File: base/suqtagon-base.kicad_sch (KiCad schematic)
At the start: 24 parts, among them J1 USB_C_Receptacle_USB2.0, J2 Conn_01x02_Male, J3 Conn_01x02_Male, J4 Conn_01x02_Male, J5 Conn_01x02_Male, J6 Conn_01x02_Male, SW1 SW_Push, SW2 SW_Push, U1 AMS1117-3.3

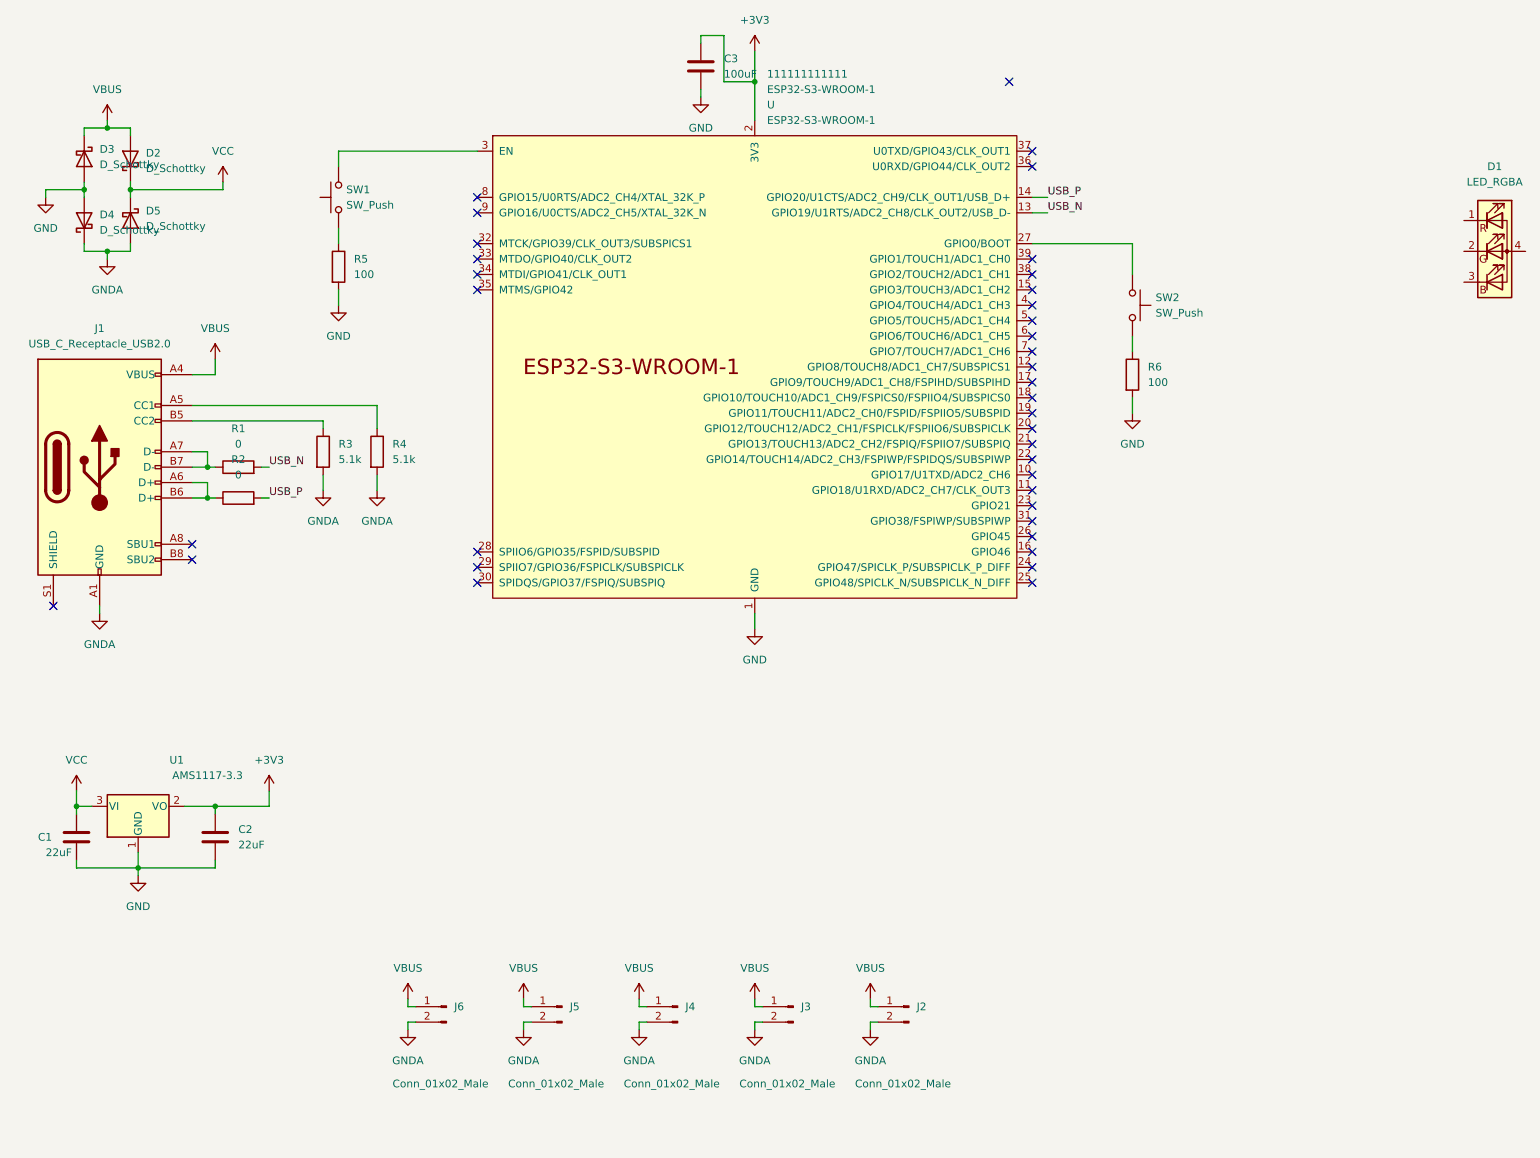
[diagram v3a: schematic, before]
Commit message: started adding hand solder footprints
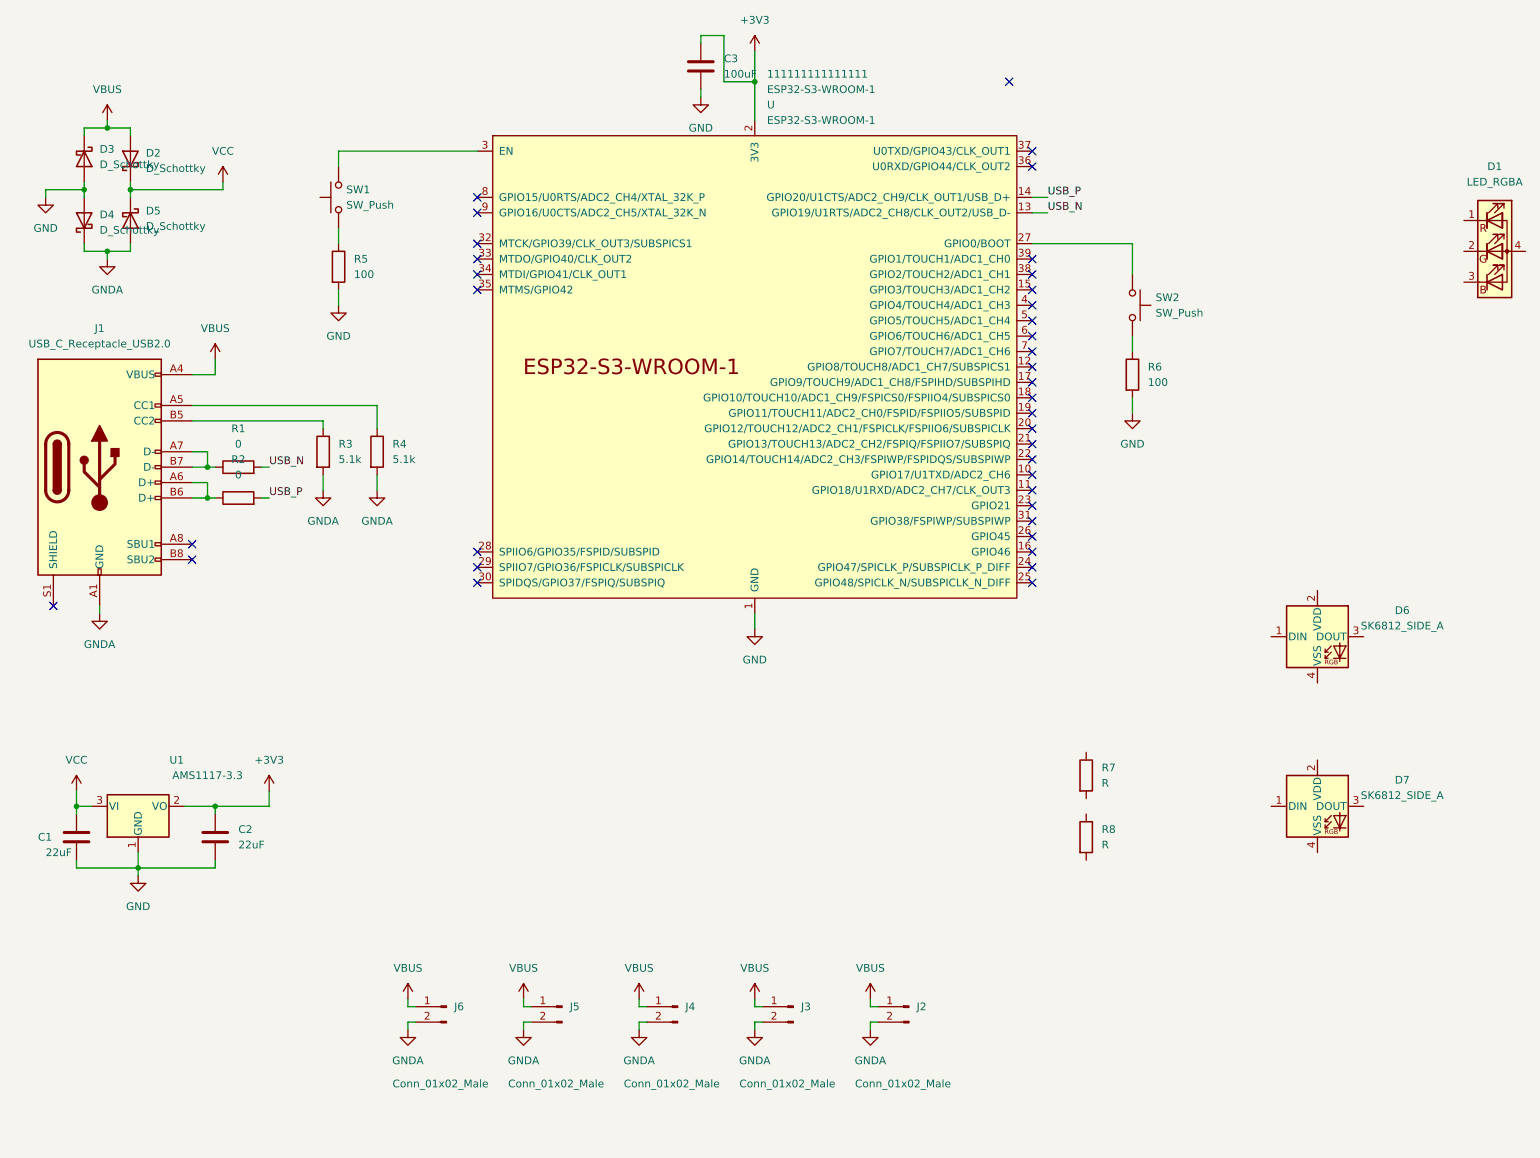
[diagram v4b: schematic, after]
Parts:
- added D6, D7: SK6812_SIDE_A, LED_SMD_SIDE:LED_SMD_SK6812_SIDE_A_4020, symbol LED_Side:SK6812_SIDE_A
- added R7: R, Resistor_SMD:R_0805_2012Metric, symbol Device:R
- added R8: R, Resistor_SMD:R_0805_2012Metric_Pad1.20x1.40mm_HandSolder, symbol Device:R
- renumbered 111111111111 to 111111111111111
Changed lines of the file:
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@@
     (effects (font (size 1.27 1.27)) (justify left bottom))
+  )
+  (symbol (lib_id "LED_Side:SK6812_SIDE_A") (at 232.41 114.3 0) (unit 1)
+    (in_bom yes) (on_board yes) (fields_autoplaced)
+    (property "Reference" "D6" (id 0) (at 246.38 109.9693 0))
+    (property "Value" "SK6812_SIDE_A" (id 1) (at 246.38 112.5093 0))
+    (property "Footprint" "LED_SMD_SIDE:LED_SMD_SK6812_SIDE_A_4020" (id 2) (at 233.68 121.92 0)
+      (effects (font (size 1.27 1.27)) (justify left top) hide)
+    )
+    (property "Datasheet" "http://www.normandled.com/upload/201810/SK6812%20SIDE-A%20LED%20Datasheet.pdf" (id 3) (at 234.95 123.825 0)
+      (effects (font (size 1.27 1.27)) (justify left top) hide)
+    )
+    (pin "1")
+    (pin "2")
+    (pin "3")
+    (pin "4")
   )
   (symbol (lib_id "power:GNDA") (at 68.58 90.17 0) (unit 1)
@@
     (pin "2")
   )
+  (symbol (lib_id "Device:R") (at 194.31 137.16 0) (unit 1)
+    (in_bom yes) (on_board yes) (fields_autoplaced)
+    (property "Reference" "R7" (id 0) (at 196.85 135.8899 0)
+      (effects (font (size 1.27 1.27)) (justify left))
+    )
+    (property "Value" "R" (id 1) (at 196.85 138.4299 0)
+      (effects (font (size 1.27 1.27)) (justify left))
+    )
+    (property "Footprint" "Resistor_SMD:R_0805_2012Metric" (id 2) (at 192.532 137.16 90)
+      (effects (font (size 1.27 1.27)) hide)
+    )
+    (property "Datasheet" "~" (id 3) (at 194.31 137.16 0)
+      (effects (font (size 1.27 1.27)) hide)
+    )
+    (pin "1")
+    (pin "2")
+  )
   (symbol (lib_id "power:VCC") (at 52.07 39.37 0) (unit 1)
     (in_bom yes) (on_board yes) (fields_autoplaced)
@@
     (pin "2")
   )
+  (symbol (lib_id "Device:R") (at 194.31 147.32 0) (unit 1)
+    (in_bom yes) (on_board yes) (fields_autoplaced)
+    (property "Reference" "R8" (id 0) (at 196.85 146.0499 0)
+      (effects (font (size 1.27 1.27)) (justify left))
+    )
+    (property "Value" "R" (id 1) (at 196.85 148.5899 0)
+      (effects (font (size 1.27 1.27)) (justify left))
+    )
+    (property "Footprint" "Resistor_SMD:R_0805_2012Metric_Pad1.20x1.40mm_HandSolder" (id 2) (at 192.532 147.32 90)
+      (effects (font (size 1.27 1.27)) hide)
+    )
+    (property "Datasheet" "~" (id 3) (at 194.31 147.32 0)
+      (effects (font (size 1.27 1.27)) hide)
+    )
+    (pin "1")
+    (pin "2")
+  )
   (symbol (lib_id "power:VBUS") (at 101.6 173.99 0) (unit 1)
     (in_bom yes) (on_board yes) (fields_autoplaced)
@@
   (symbol (lib_id "Espressif:ESP32-S3-WROOM-1") (at 139.7 69.85 0) (unit 1)
     (in_bom yes) (on_board yes) (fields_autoplaced)
-    (property "Reference" "111111111111" (id 0) (at 141.7194 21.59 0)
+    (property "Reference" "111111111111111" (id 0) (at 141.7194 21.59 0)
       (effects (font (size 1.27 1.27)) (justify left))
     )
@@
     (pin "2")
   )
+  (symbol (lib_id "LED_Side:SK6812_SIDE_A") (at 232.41 142.24 0) (unit 1)
+    (in_bom yes) (on_board yes) (fields_autoplaced)
+    (property "Reference" "D7" (id 0) (at 246.38 137.9093 0))
+    (property "Value" "SK6812_SIDE_A" (id 1) (at 246.38 140.4493 0))
+    (property "Footprint" "LED_SMD_SIDE:LED_SMD_SK6812_SIDE_A_4020" (id 2) (at 233.68 149.86 0)
+      (effects (font (size 1.27 1.27)) (justify left top) hide)
+    )
+    (property "Datasheet" "http://www.normandled.com/upload/201810/SK6812%20SIDE-A%20LED%20Datasheet.pdf" (id 3) (at 234.95 151.765 0)
+      (effects (font (size 1.27 1.27)) (justify left top) hide)
+    )
+    (pin "1")
+    (pin "2")
+    (pin "3")
+    (pin "4")
+  )
   (symbol (lib_id "Connector:Conn_01x02_Male") (at 127 175.26 0) (mirror y) (unit 1)
     (in_bom yes) (on_board yes)
@@
     )
     (path "/761644a8-58a9-4bb2-8003-7f19d43a1827"
-      (reference "111111111111") (unit 1) (value "ESP32-S3-WROOM-1") (footprint "Espressif:ESP32-S3-WROOM-1U")
+      (reference "111111111111111") (unit 1) (value "ESP32-S3-WROOM-1") (footprint "Espressif:ESP32-S3-WROOM-1U")
     )
     (path "/1062990a-607a-4b52-b57c-c444e6f10a17"
@@
       (reference "D5") (unit 1) (value "D_Schottky") (footprint "Diode_SMD:D_SMB")
     )
+    (path "/05584861-80b0-4823-89c5-d677033aeb10"
+      (reference "D6") (unit 1) (value "SK6812_SIDE_A") (footprint "LED_SMD_SIDE:LED_SMD_SK6812_SIDE_A_4020")
+    )
+    (path "/dac5b6f8-e0f5-4896-bd9d-ba13c95e5a2b"
+      (reference "D7") (unit 1) (value "SK6812_SIDE_A") (footprint "LED_SMD_SIDE:LED_SMD_SK6812_SIDE_A_4020")
+    )
     (path "/d1f6cfad-2a05-4c1b-99fc-73c0e2e6741a"
       (reference "J1") (unit 1) (value "USB_C_Receptacle_USB2.0") (footprint "Connector_USB:USB_C_Receptacle_HRO_TYPE-C-31-M-12")
@@
       (reference "R6") (unit 1) (value "100") (footprint "Resistor_SMD:R_0805_2012Metric_Pad1.20x1.40mm_HandSolder")
     )
+    (path "/09669309-32ea-4a5f-92b3-fed51f6e2892"
+      (reference "R7") (unit 1) (value "R") (footprint "Resistor_SMD:R_0805_2012Metric")
+    )
+    (path "/598a8726-a9f0-4383-83de-07a648077382"
+      (reference "R8") (unit 1) (value "R") (footprint "Resistor_SMD:R_0805_2012Metric_Pad1.20x1.40mm_HandSolder")
+    )
     (path "/b1083b2b-afcd-4f5b-a5a9-2da0cdfd2a2f"

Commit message: test background eb
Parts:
- removed R7: R, Resistor_SMD:R_0805_2012Metric, symbol Device:R
- removed R8: R, Resistor_SMD:R_0805_2012Metric_Pad1.20x1.40mm_HandSolder, symbol Device:R
- D6, D7: footprint LED_SMD_SIDE:LED_SMD_SK6812_SIDE_A_4020 -> LED_SMD_SIDE:LED_SMD_SK6812_SIDE_A_4020_HandSolder
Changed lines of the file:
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@@
     (property "Reference" "D6" (id 0) (at 246.38 109.9693 0))
     (property "Value" "SK6812_SIDE_A" (id 1) (at 246.38 112.5093 0))
-    (property "Footprint" "LED_SMD_SIDE:LED_SMD_SK6812_SIDE_A_4020" (id 2) (at 233.68 121.92 0)
+    (property "Footprint" "LED_SMD_SIDE:LED_SMD_SK6812_SIDE_A_4020_HandSolder" (id 2) (at 233.68 121.92 0)
       (effects (font (size 1.27 1.27)) (justify left top) hide)
     )
@@
     (pin "2")
   )
-  (symbol (lib_id "Device:R") (at 194.31 137.16 0) (unit 1)
-    (in_bom yes) (on_board yes) (fields_autoplaced)
-    (property "Reference" "R7" (id 0) (at 196.85 135.8899 0)
-      (effects (font (size 1.27 1.27)) (justify left))
-    )
-    (property "Value" "R" (id 1) (at 196.85 138.4299 0)
-      (effects (font (size 1.27 1.27)) (justify left))
-    )
-    (property "Footprint" "Resistor_SMD:R_0805_2012Metric" (id 2) (at 192.532 137.16 90)
-      (effects (font (size 1.27 1.27)) hide)
-    )
-    (property "Datasheet" "~" (id 3) (at 194.31 137.16 0)
-      (effects (font (size 1.27 1.27)) hide)
-    )
-    (pin "1")
-    (pin "2")
-  )
   (symbol (lib_id "power:VCC") (at 52.07 39.37 0) (unit 1)
     (in_bom yes) (on_board yes) (fields_autoplaced)
@@
     )
     (property "Datasheet" "~" (id 3) (at 77.47 83.82 0)
-      (effects (font (size 1.27 1.27)) hide)
-    )
-    (pin "1")
-    (pin "2")
-  )
-  (symbol (lib_id "Device:R") (at 194.31 147.32 0) (unit 1)
-    (in_bom yes) (on_board yes) (fields_autoplaced)
-    (property "Reference" "R8" (id 0) (at 196.85 146.0499 0)
-      (effects (font (size 1.27 1.27)) (justify left))
-    )
-    (property "Value" "R" (id 1) (at 196.85 148.5899 0)
-      (effects (font (size 1.27 1.27)) (justify left))
-    )
-    (property "Footprint" "Resistor_SMD:R_0805_2012Metric_Pad1.20x1.40mm_HandSolder" (id 2) (at 192.532 147.32 90)
-      (effects (font (size 1.27 1.27)) hide)
-    )
-    (property "Datasheet" "~" (id 3) (at 194.31 147.32 0)
       (effects (font (size 1.27 1.27)) hide)
     )
@@
     (property "Reference" "D7" (id 0) (at 246.38 137.9093 0))
     (property "Value" "SK6812_SIDE_A" (id 1) (at 246.38 140.4493 0))
-    (property "Footprint" "LED_SMD_SIDE:LED_SMD_SK6812_SIDE_A_4020" (id 2) (at 233.68 149.86 0)
+    (property "Footprint" "LED_SMD_SIDE:LED_SMD_SK6812_SIDE_A_4020_HandSolder" (id 2) (at 233.68 149.86 0)
       (effects (font (size 1.27 1.27)) (justify left top) hide)
     )
@@
     )
     (path "/05584861-80b0-4823-89c5-d677033aeb10"
-      (reference "D6") (unit 1) (value "SK6812_SIDE_A") (footprint "LED_SMD_SIDE:LED_SMD_SK6812_SIDE_A_4020")
+      (reference "D6") (unit 1) (value "SK6812_SIDE_A") (footprint "LED_SMD_SIDE:LED_SMD_SK6812_SIDE_A_4020_HandSolder")
     )
     (path "/dac5b6f8-e0f5-4896-bd9d-ba13c95e5a2b"
-      (reference "D7") (unit 1) (value "SK6812_SIDE_A") (footprint "LED_SMD_SIDE:LED_SMD_SK6812_SIDE_A_4020")
+      (reference "D7") (unit 1) (value "SK6812_SIDE_A") (footprint "LED_SMD_SIDE:LED_SMD_SK6812_SIDE_A_4020_HandSolder")
     )
     (path "/d1f6cfad-2a05-4c1b-99fc-73c0e2e6741a"
@@
       (reference "R6") (unit 1) (value "100") (footprint "Resistor_SMD:R_0805_2012Metric_Pad1.20x1.40mm_HandSolder")
     )
-    (path "/09669309-32ea-4a5f-92b3-fed51f6e2892"
-      (reference "R7") (unit 1) (value "R") (footprint "Resistor_SMD:R_0805_2012Metric")
-    )
-    (path "/598a8726-a9f0-4383-83de-07a648077382"
-      (reference "R8") (unit 1) (value "R") (footprint "Resistor_SMD:R_0805_2012Metric_Pad1.20x1.40mm_HandSolder")
-    )
     (path "/b1083b2b-afcd-4f5b-a5a9-2da0cdfd2a2f"
